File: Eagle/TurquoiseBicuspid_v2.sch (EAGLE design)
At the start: 19 parts, among them J0 0Ω, J1 10118192-0001LF, J2 0Ω

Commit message: added frame
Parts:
- C2: value 0.1µf -> 10µf
- renumbered J1 to USB
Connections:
- removed net N$3: HM-10.GND1, J0.2
- net GND: now also HM-10.GND1, HM-10.GND2, HM-10.GND3, HM-10.GND4, J0.2
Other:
- note added: "1"
- note added: "2.0.0"
- note added: "Designed by: Jared De La Cruz jared@jareddlc.com"

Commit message: fixed pulldown resistor
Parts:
- C2: value 10µf -> 0.1µf
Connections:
- removed net N$1: HM-10.UART_TX, R5.2
- removed net N$2: HM-10.UART_RX, R6.2
- net BT_RX: now also HM-10.UART_RX, R6.2; no longer R6.1
- net BT_TX: now also HM-10.UART_TX, R5.2; no longer R5.1
- net GND: now also R5.1, R6.1
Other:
- moved on the sheet: R5, R6
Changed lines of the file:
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@@
 <setting verticaltext="up"/>
 </settings>
-<grid distance="0.1" unitdist="mm" unit="mm" style="lines" multiple="1" display="no" altdistance="0.01" altunitdist="inch" altunit="inch"/>
+<grid distance="0.1" unitdist="inch" unit="inch" style="lines" multiple="1" display="no" altdistance="0.01" altunitdist="inch" altunit="inch"/>
 <layers>
 <layer number="1" name="Top" color="4" fill="1" visible="no" active="no"/>
@@
 <part name="USB" library="fci_micro_usb" deviceset="10118192-0001LF" device=""/>
 <part name="ATTINY85" library="attiny85" deviceset="ATTINY85" device="SU"/>
-<part name="C2" library="rcl" deviceset="C-EU" device="C1206" value="10µf"/>
+<part name="C2" library="rcl" deviceset="C-EU" device="C1206" value="0.1µf"/>
 <part name="C3" library="rcl" deviceset="C-EU" device="C1206" value="10µf"/>
 <part name="FRAME1" library="frames" deviceset="LETTER_L" device="">
@@
 <instance part="J0" gate="G$1" x="48.26" y="-17.78" rot="R90"/>
 <instance part="J2" gate="G$1" x="48.26" y="43.18"/>
-<instance part="R5" gate="G$1" x="35.56" y="27.94"/>
-<instance part="R6" gate="G$1" x="45.72" y="25.4"/>
+<instance part="R5" gate="G$1" x="38.1" y="17.78" rot="R90"/>
+<instance part="R6" gate="G$1" x="45.72" y="17.78" rot="R90"/>
 <instance part="HM-10" gate="G$1" x="58.42" y="38.1"/>
 <instance part="USB" gate="G$1" x="-30.48" y="17.78" smashed="yes">
@@
 <pinref part="C1" gate="G$1" pin="2"/>
 <wire x1="-20.32" y1="-25.4" x2="-15.24" y2="-25.4" width="0.1524" layer="91"/>
-<wire x1="-15.24" y1="-25.4" x2="43.18" y2="-25.4" width="0.1524" layer="91"/>
+<wire x1="-15.24" y1="-25.4" x2="38.1" y2="-25.4" width="0.1524" layer="91"/>
+<wire x1="38.1" y1="-25.4" x2="40.64" y2="-25.4" width="0.1524" layer="91"/>
+<wire x1="40.64" y1="-25.4" x2="43.18" y2="-25.4" width="0.1524" layer="91"/>
 <wire x1="43.18" y1="-25.4" x2="43.18" y2="-7.62" width="0.1524" layer="91"/>
 <wire x1="-15.24" y1="10.16" x2="-15.24" y2="-5.08" width="0.1524" layer="91"/>
@@
 <wire x1="86.36" y1="-2.54" x2="96.52" y2="-2.54" width="0.1524" layer="91"/>
 <junction x="96.52" y="-2.54"/>
+<pinref part="R6" gate="G$1" pin="1"/>
+<wire x1="45.72" y1="12.7" x2="45.72" y2="5.08" width="0.1524" layer="91"/>
+<wire x1="45.72" y1="5.08" x2="40.64" y2="5.08" width="0.1524" layer="91"/>
+<wire x1="40.64" y1="5.08" x2="40.64" y2="-25.4" width="0.1524" layer="91"/>
+<junction x="40.64" y="-25.4"/>
+<pinref part="R5" gate="G$1" pin="1"/>
+<wire x1="38.1" y1="12.7" x2="38.1" y2="-25.4" width="0.1524" layer="91"/>
+<junction x="38.1" y="-25.4"/>
 </segment>
 <segment>
@@
 <wire x1="27.94" y1="15.24" x2="27.94" y2="27.94" width="0.1524" layer="91"/>
 <wire x1="17.78" y1="15.24" x2="27.94" y2="15.24" width="0.1524" layer="91"/>
-<pinref part="R5" gate="G$1" pin="1"/>
-<wire x1="27.94" y1="27.94" x2="30.48" y2="27.94" width="0.1524" layer="91"/>
 <pinref part="ATTINY85" gate="G$1" pin="PB2"/>
+<pinref part="HM-10" gate="G$1" pin="UART_TX"/>
+<wire x1="27.94" y1="27.94" x2="38.1" y2="27.94" width="0.1524" layer="91"/>
+<pinref part="R5" gate="G$1" pin="2"/>
+<wire x1="38.1" y1="27.94" x2="53.34" y2="27.94" width="0.1524" layer="91"/>
+<wire x1="38.1" y1="27.94" x2="38.1" y2="22.86" width="0.1524" layer="91"/>
+<junction x="38.1" y="27.94"/>
 </segment>
 </net>
@@
 <segment>
 <wire x1="30.48" y1="17.78" x2="17.78" y2="17.78" width="0.1524" layer="91"/>
-<pinref part="R6" gate="G$1" pin="1"/>
 <wire x1="30.48" y1="17.78" x2="30.48" y2="25.4" width="0.1524" layer="91"/>
-<wire x1="30.48" y1="25.4" x2="40.64" y2="25.4" width="0.1524" layer="91"/>
 <pinref part="ATTINY85" gate="G$1" pin="PB3"/>
+<pinref part="HM-10" gate="G$1" pin="UART_RX"/>
+<wire x1="30.48" y1="25.4" x2="45.72" y2="25.4" width="0.1524" layer="91"/>
+<pinref part="R6" gate="G$1" pin="2"/>
+<wire x1="45.72" y1="25.4" x2="53.34" y2="25.4" width="0.1524" layer="91"/>
+<wire x1="45.72" y1="25.4" x2="45.72" y2="22.86" width="0.1524" layer="91"/>
+<junction x="45.72" y="25.4"/>
 </segment>
 </net>
@@
 </segment>
 </net>
-<net name="N$2" class="0">
-<segment>
-<pinref part="R6" gate="G$1" pin="2"/>
-<pinref part="HM-10" gate="G$1" pin="UART_RX"/>
-<wire x1="50.8" y1="25.4" x2="53.34" y2="25.4" width="0.1524" layer="91"/>
-</segment>
-</net>
-<net name="N$1" class="0">
-<segment>
-<pinref part="R5" gate="G$1" pin="2"/>
-<pinref part="HM-10" gate="G$1" pin="UART_TX"/>
-<wire x1="40.64" y1="27.94" x2="53.34" y2="27.94" width="0.1524" layer="91"/>
-</segment>
-</net>

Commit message: connecting routes
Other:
- note added: "Schematic"
- note removed: "1"
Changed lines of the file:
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@@
 <plain>
 <text x="144.78" y="-71.12" size="2.54" layer="94" font="vector" align="bottom-center">2.0.0</text>
-<text x="96.52" y="-68.58" size="2.54" layer="94" font="vector" align="bottom-center">1</text>
 <text x="88.9" y="-53.34" size="2.54" layer="94" font="vector" align="bottom-center">Designed by:    Jared De La Cruz
                 jared@jareddlc.com</text>
+<text x="91.44" y="-68.58" size="2.54" layer="94">Schematic</text>
 </plain>
 <instances>

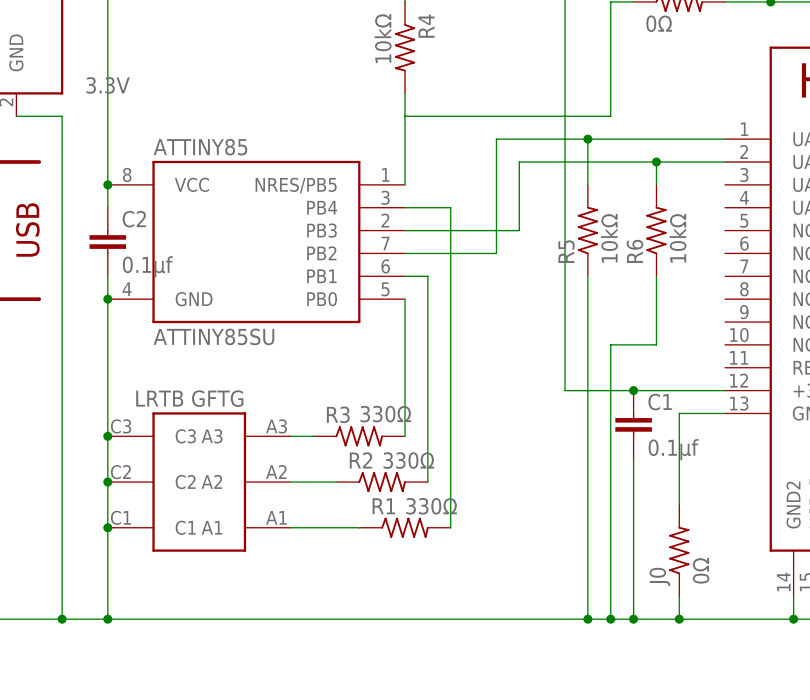
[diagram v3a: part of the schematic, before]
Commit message: re-routed pins for RX & TX
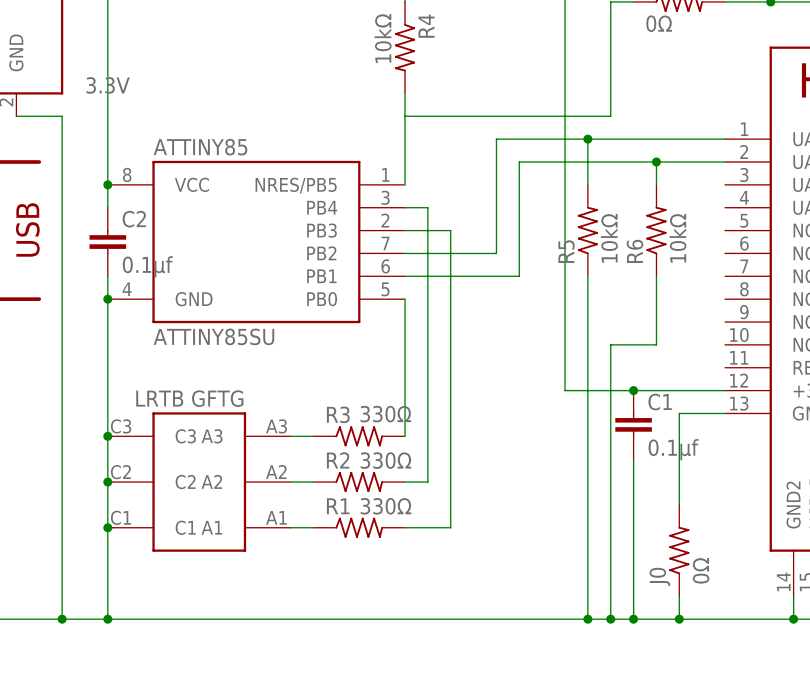
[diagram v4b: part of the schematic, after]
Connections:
- net A1: now also ATTINY85.PB3; no longer ATTINY85.PB4
- net A2: now also ATTINY85.PB4; no longer ATTINY85.PB1
- net BT_RX: now also ATTINY85.PB1; no longer ATTINY85.PB3
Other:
- moved on the sheet: R1, R2
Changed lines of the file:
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@@
 <instance part="C1" gate="G$1" x="43.18" y="-2.54"/>
 <instance part="3.3VREG" gate="G1" x="-27.94" y="40.64"/>
-<instance part="R1" gate="G$1" x="17.78" y="-15.24" smashed="yes">
-<attribute name="NAME" x="13.97" y="-13.7414" size="1.778" layer="95"/>
-<attribute name="VALUE" x="17.77" y="-13.742" size="1.778" layer="96"/>
-</instance>
-<instance part="R2" gate="G$1" x="15.24" y="-10.16" smashed="yes">
-<attribute name="NAME" x="11.43" y="-8.6614" size="1.778" layer="95"/>
-<attribute name="VALUE" x="15.23" y="-8.662" size="1.778" layer="96"/>
+<instance part="R1" gate="G$1" x="12.7" y="-15.24" smashed="yes">
+<attribute name="NAME" x="8.89" y="-13.7414" size="1.778" layer="95"/>
+<attribute name="VALUE" x="12.69" y="-13.742" size="1.778" layer="96"/>
+</instance>
+<instance part="R2" gate="G$1" x="12.7" y="-10.16" smashed="yes">
+<attribute name="NAME" x="8.89" y="-8.6614" size="1.778" layer="95"/>
+<attribute name="VALUE" x="12.69" y="-8.662" size="1.778" layer="96"/>
 </instance>
 <instance part="R3" gate="G$1" x="12.7" y="-5.08" smashed="yes">
@@
 <net name="A2" class="0">
 <segment>
-<wire x1="20.32" y1="12.7" x2="20.32" y2="-10.16" width="0.1524" layer="91"/>
-<wire x1="17.78" y1="12.7" x2="20.32" y2="12.7" width="0.1524" layer="91"/>
-<pinref part="R2" gate="G$1" pin="2"/>
-<pinref part="ATTINY85" gate="G$1" pin="PB1"/>
-</segment>
-<segment>
 <pinref part="U$1" gate="G$1" pin="A2"/>
 <pinref part="R2" gate="G$1" pin="1"/>
-<wire x1="5.08" y1="-10.16" x2="10.16" y2="-10.16" width="0.1524" layer="91"/>
+<wire x1="5.08" y1="-10.16" x2="7.62" y2="-10.16" width="0.1524" layer="91"/>
+</segment>
+<segment>
+<wire x1="20.32" y1="-10.16" x2="17.78" y2="-10.16" width="0.1524" layer="91"/>
+<pinref part="R2" gate="G$1" pin="2"/>
+<wire x1="20.32" y1="-10.16" x2="20.32" y2="20.32" width="0.1524" layer="91"/>
+<pinref part="ATTINY85" gate="G$1" pin="PB4"/>
+<wire x1="20.32" y1="20.32" x2="17.78" y2="20.32" width="0.1524" layer="91"/>
 </segment>
 </net>
@@
 <segment>
 <pinref part="U$1" gate="G$1" pin="A1"/>
-<wire x1="12.7" y1="-15.24" x2="5.08" y2="-15.24" width="0.1524" layer="91"/>
+<wire x1="7.62" y1="-15.24" x2="5.08" y2="-15.24" width="0.1524" layer="91"/>
 <pinref part="R1" gate="G$1" pin="1"/>
 </segment>
 <segment>
-<wire x1="17.78" y1="20.32" x2="22.86" y2="20.32" width="0.1524" layer="91"/>
-<wire x1="22.86" y1="20.32" x2="22.86" y2="-15.24" width="0.1524" layer="91"/>
+<pinref part="ATTINY85" gate="G$1" pin="PB3"/>
+<wire x1="22.86" y1="17.78" x2="17.78" y2="17.78" width="0.1524" layer="91"/>
 <pinref part="R1" gate="G$1" pin="2"/>
-<pinref part="ATTINY85" gate="G$1" pin="PB4"/>
+<wire x1="17.78" y1="-15.24" x2="22.86" y2="-15.24" width="0.1524" layer="91"/>
+<wire x1="22.86" y1="-15.24" x2="22.86" y2="17.78" width="0.1524" layer="91"/>
 </segment>
 </net>
@@
 <net name="BT_RX" class="0">
 <segment>
-<wire x1="30.48" y1="17.78" x2="17.78" y2="17.78" width="0.1524" layer="91"/>
-<wire x1="30.48" y1="17.78" x2="30.48" y2="25.4" width="0.1524" layer="91"/>
-<pinref part="ATTINY85" gate="G$1" pin="PB3"/>
+<wire x1="30.48" y1="12.7" x2="30.48" y2="25.4" width="0.1524" layer="91"/>
 <pinref part="HM-10" gate="G$1" pin="UART_RX"/>
 <wire x1="30.48" y1="25.4" x2="45.72" y2="25.4" width="0.1524" layer="91"/>
@@
 <wire x1="45.72" y1="25.4" x2="45.72" y2="22.86" width="0.1524" layer="91"/>
 <junction x="45.72" y="25.4"/>
-</segment>
-</net>
+<pinref part="ATTINY85" gate="G$1" pin="PB1"/>
+<wire x1="30.48" y1="12.7" x2="17.78" y2="12.7" width="0.1524" layer="91"/>
+</segment>
+</net>

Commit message: board design v2
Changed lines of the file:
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@@
 <wire x1="40.64" y1="43.18" x2="43.18" y2="43.18" width="0.1524" layer="91"/>
 <pinref part="ATTINY85" gate="G$1" pin="NRES/PB5"/>
+<junction x="17.78" y="30.48"/>
 </segment>
 <segment>
